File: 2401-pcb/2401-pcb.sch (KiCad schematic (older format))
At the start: 100 parts, among them J1 Load Cell, J2 Conn_ARM_JTAG_SWD_10, J3 Conn_01x04_Male, Q1 SFH3710, Q2 SFH3710, SW1 SW_SPDT, U1 LIS3DH, U10 MCP6001U, U11 MCP6001U, U2 VL6180X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

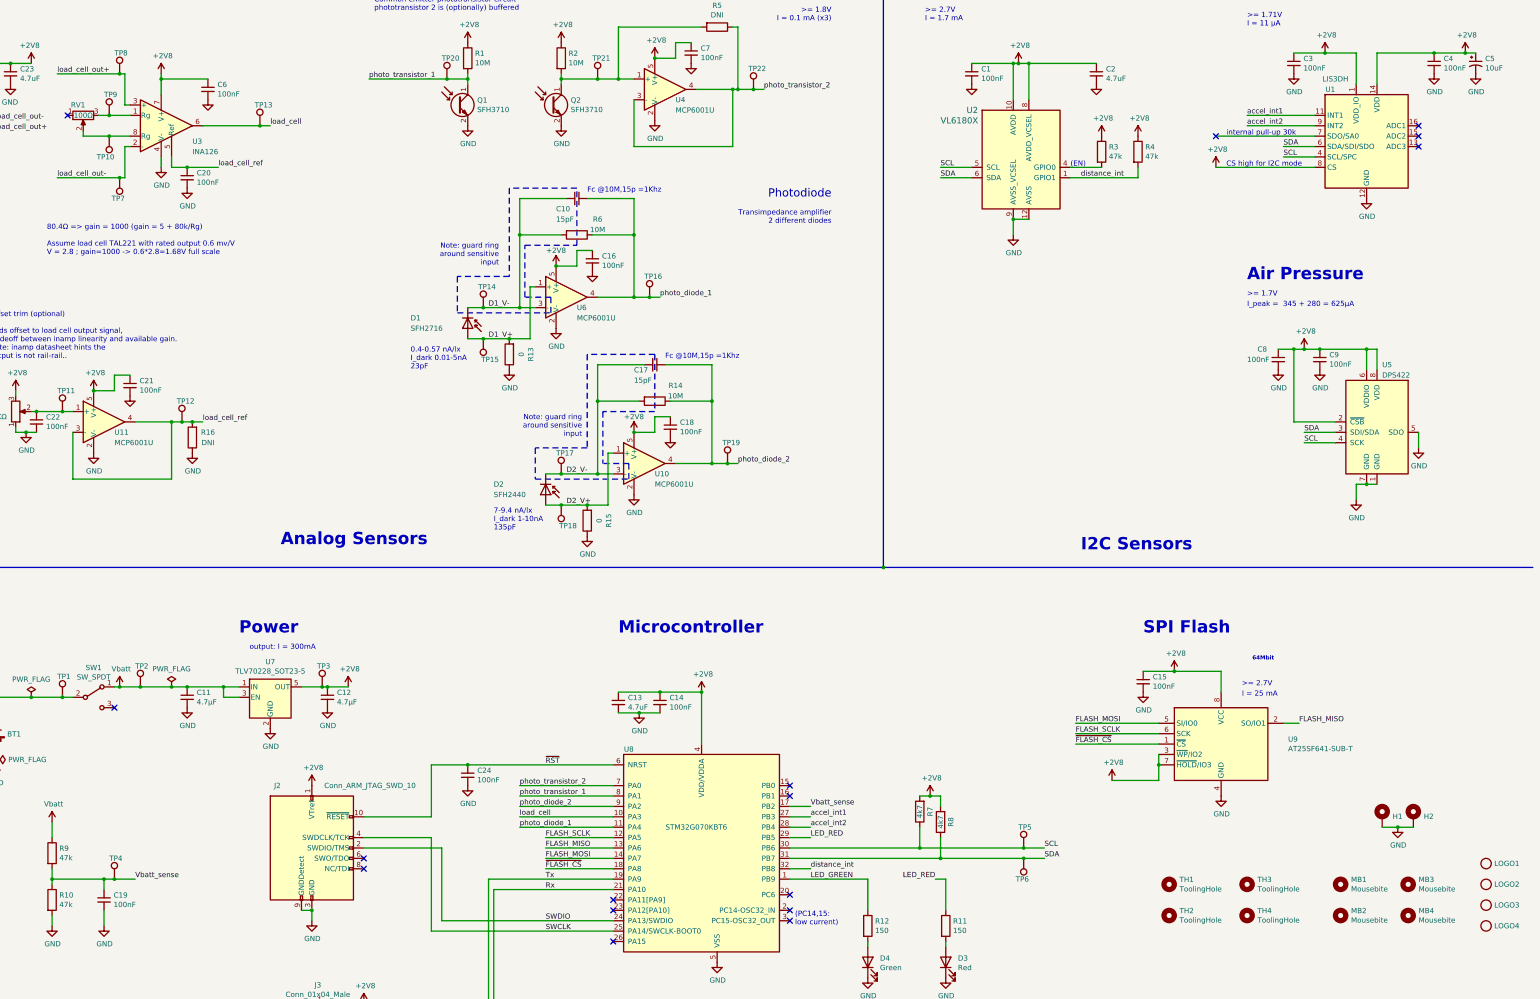
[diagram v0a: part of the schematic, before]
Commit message: PCB: add Final production BOM
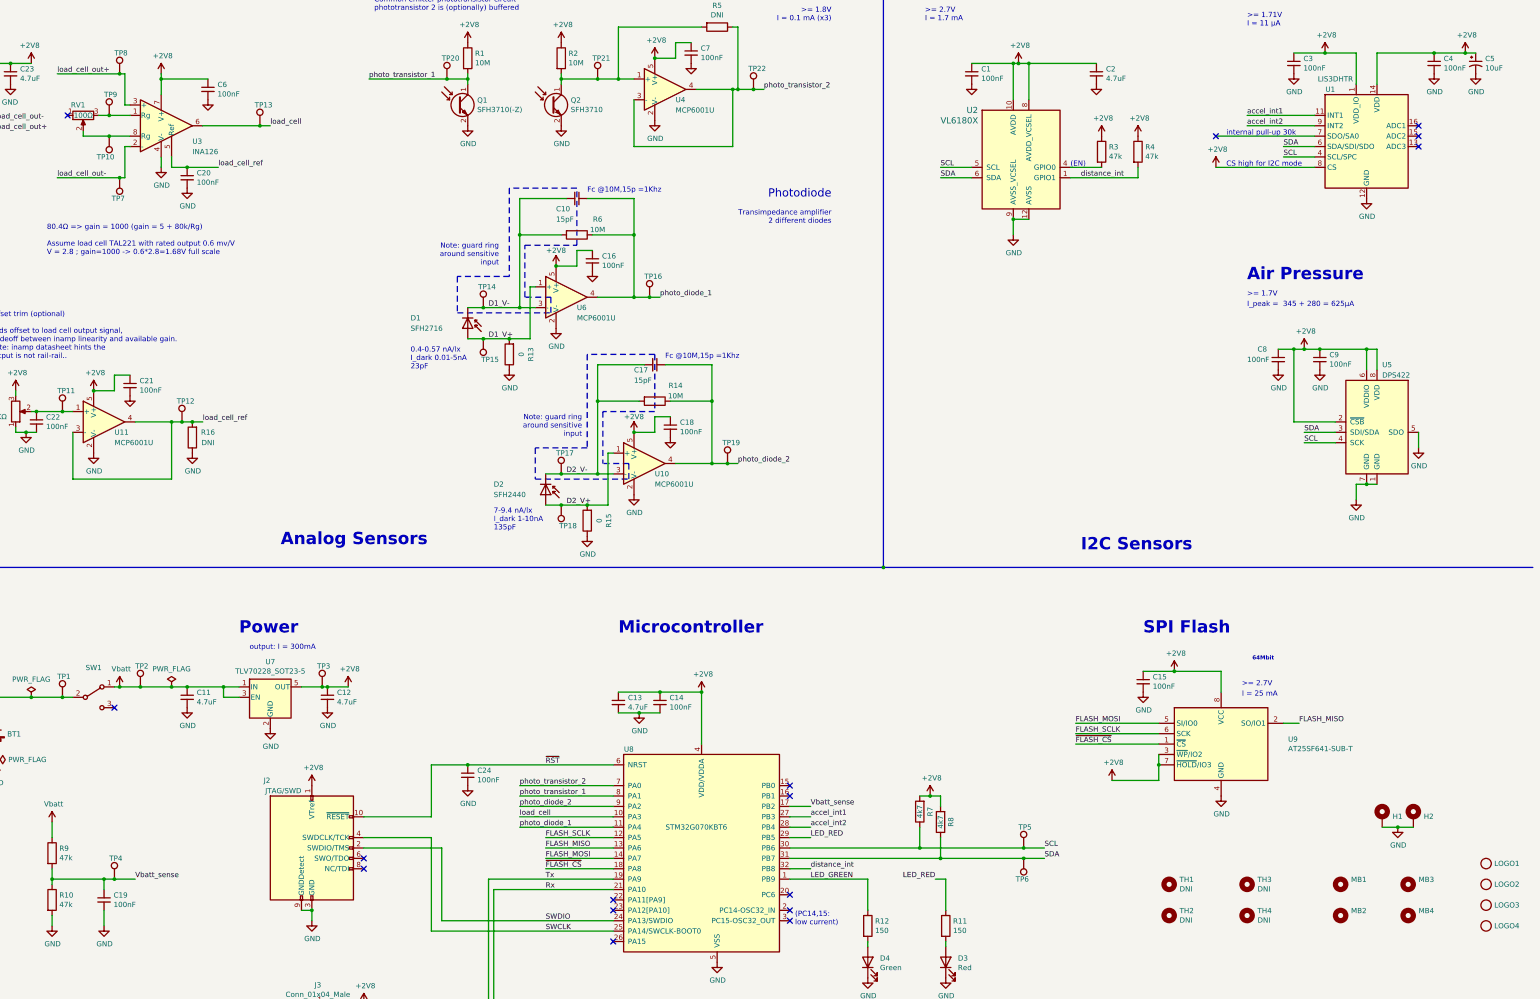
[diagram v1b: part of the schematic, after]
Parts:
- C11, C12: value 4.7µF -> 4.7uF
- D1: Farnell (none) -> 2981722; MPN (none) -> SFH 2716
- D2: Farnell (none) -> 2981709; MPN (none) -> SFH 2440
- H1, H2: value MountingHole_Pad -> DNI
- J1: Farnell (none) -> 9492631; MPN (none) -> S4B-PH-SM4-TB(LF)(SN)
- J2: value Conn_ARM_JTAG_SWD_10 -> JTAG/SWD; MPN (none) -> 20021521-00010T1LF; Note (none) -> Jitter has large amount in stock..
- LOGO1, LOGO2, LOGO3, LOGO4: value LOGO -> DNI
- MB1, MB2, MB3, MB4: value Mousebite -> DNI
- Q1: value SFH3710 -> SFH3710(-Z); Alternative (none) -> SFH3710; Farnell (none) -> 2981749; MPN (none) -> SFH3710-Z
- Q2: Farnell (none) -> 1573490; MPN (none) -> SFH3710
- SW1: Farnell (none) -> 1608080; MPN (none) -> 09.03201.02
- TH1, TH2, TH3, TH4: value ToolingHole -> DNI
- U1: value LIS3DH -> LIS3DHTR; Farnell (none) -> 2253507; MPN (none) -> LIS3DHTR; Mouser (none) -> 511-LIS3DHTR; NOTE (none) -> NOT the same as LIS3DHH !!
- U2: Farnell (none) -> 2462820; MPN (none) -> VL6180XV0NR/1
- U3: MPN (none) -> INA126E
- U5: Farnell (none) -> 2986299; MPN (none) -> DPS422XTSA1
- U7: Farnell (none) -> 2492371; MPN (none) -> TLV70228DBVT
- U8: Farnell (none) -> 3365394; MPN (none) -> STM32G070KBT6; Mouser (none) -> 511-STM32G070KBT6
- U9: Farnell (none) -> 2988514; MPN (none) -> AT25SF641-SUB-T
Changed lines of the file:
@@
 F 2 "Package_SO:SOIC-8_3.9x4.9mm_P1.27mm" H 13050 7450 50  0001 C CNN
 F 3 "http://www.farnell.com/datasheets/2720345.pdf" H 13050 8050 50  0001 C CNN
+F 4 "AT25SF641-SUB-T" H 13050 8050 50  0001 C CNN "MPN"
+F 5 "2988514" H 13050 8050 50  0001 C CNN "Farnell"
 	1    13050 8050
 	1    0    0    -1
@@
 P 4450 7600
 F 0 "C12" H 4542 7646 50  0000 L CNN
-F 1 "4.7µF" H 4542 7555 50  0000 L CNN
+F 1 "4.7uF" H 4542 7555 50  0000 L CNN
 F 2 "Capacitor_SMD:C_0805_2012Metric" H 4450 7600 50  0001 C CNN
 F 3 "~" H 4450 7600 50  0001 C CNN
@@
 P 3100 7600
 F 0 "C11" H 3192 7646 50  0000 L CNN
-F 1 "4.7µF" H 3192 7555 50  0000 L CNN
+F 1 "4.7uF" H 3192 7555 50  0000 L CNN
 F 2 "Capacitor_SMD:C_0805_2012Metric" H 3100 7600 50  0001 C CNN
 F 3 "~" H 3100 7600 50  0001 C CNN
@@
 F 2 "Package_TO_SOT_SMD:SOT-23-5" H 3900 7925 50  0001 C CIN
 F 3 "http://www.ti.com/lit/ds/symlink/tlv702.pdf" H 3900 7650 50  0001 C CNN
+F 4 "TLV70228DBVT" H 3900 7600 50  0001 C CNN "MPN"
+F 5 "2492371" H 3900 7600 50  0001 C CNN "Farnell"
 	1    3900 7600
 	1    0    0    -1
@@
 P 2200 7600
 F 0 "SW1" H 2200 7885 50  0000 C CNN
-F 1 "SW_SPDT" H 2200 7794 50  0000 C CNN
+F 1 "SW_SPDT" H 2200 7794 50  0001 C CNN
 F 2 "Jitter_Footprints:slide_switch_09.03201.02" H 2200 7600 50  0001 C CNN
 F 3 "~" H 2200 7600 50  0001 C CNN
+F 4 "09.03201.02" H 2200 7600 50  0001 C CNN "MPN"
+F 5 "1608080" H 2200 7600 50  0001 C CNN "Farnell"
 	1    2200 7600
 	1    0    0    -1
@@
 U 1 1 5E58D766
 P 4300 9050
-F 0 "J2" H 4000 9650 50  0000 R CNN
-F 1 "Conn_ARM_JTAG_SWD_10" H 5300 9650 50  0000 R CNN
+F 0 "J2" H 3900 9700 50  0000 R CNN
+F 1 "JTAG/SWD" H 4200 9600 50  0000 R CNN
 F 2 "Jitter_Footprints:connector_jtag_10pin_shrouded" H 4300 9050 50  0001 C CNN
 F 3 "http://infocenter.arm.com/help/topic/com.arm.doc.ddi0314h/DDI0314H_coresight_components_trm.pdf" V 3950 7800 50  0001 C CNN
+F 4 "20021521-00010T1LF" H 4300 9050 50  0001 C CNN "MPN"
+F 5 "Jitter has large amount in stock.." H 4300 9050 50  0001 C CNN "Note"
 	1    4300 9050
 	1    0    0    -1
@@
 P 14600 8750
 F 0 "H1" H 14700 8753 50  0000 L CNN
-F 1 "MountingHole_Pad" H 14700 8708 50  0001 L CNN
+F 1 "DNI" H 14700 8708 50  0001 L CNN
 F 2 "MountingHole:MountingHole_4.5mm_Pad_Via" H 14600 8750 50  0001 C CNN
 F 3 "~" H 14600 8750 50  0001 C CNN
@@
 P 14900 8750
 F 0 "H2" H 15000 8753 50  0000 L CNN
-F 1 "MountingHole_Pad" H 15000 8708 50  0001 L CNN
+F 1 "DNI" H 15000 8708 50  0001 L CNN
 F 2 "MountingHole:MountingHole_4.5mm_Pad_Via" H 14900 8750 50  0001 C CNN
 F 3 "~" H 14900 8750 50  0001 C CNN
@@
 F 3 "https://www.st.com/resource/en/datasheet/stm32g070kb.pdf" H 8200 8850 50  0001 C CNN
 F 4 "https://www.st.com/content/ccc/resource/technical/document/reference_manual/group0/fd/a3/20/58/ac/b0/48/23/DM00463896/files/DM00463896.pdf/jcr:content/translations/en.DM00463896.pdf" H 7900 8850 50  0001 C CNN "Manual"
+F 5 "STM32G070KBT6" H 8050 8850 50  0001 C CNN "MPN"
+F 6 "511-STM32G070KBT6" H 8050 8850 50  0001 C CNN "Mouser"
+F 7 "3365394" H 8050 8850 50  0001 C CNN "Farnell"
 	1    8050 8850
 	1    0    0    -1
@@
 P 15600 9200
 F 0 "LOGO1" H 15678 9200 50  0000 L CNN
-F 1 "LOGO" H 15678 9155 50  0001 L CNN
+F 1 "DNI" H 15678 9155 50  0001 L CNN
 F 2 "Jitter_Logos:Jitter" H 15600 9200 50  0001 C CNN
 F 3 "" H 15600 9200 50  0001 C CNN
@@
 P 15600 9400
 F 0 "LOGO2" H 15678 9400 50  0000 L CNN
-F 1 "LOGO" H 15678 9355 50  0001 L CNN
+F 1 "DNI" H 15678 9355 50  0001 L CNN
 F 2 "Jitter_Logos:Symbol_Jitter-Icon_CopperAndSilkScreenTop" H 15600 9400 50  0001 C CNN
 F 3 "" H 15600 9400 50  0001 C CNN
@@
 P 14200 9400
 F 0 "MB1" H 14300 9446 50  0000 L CNN
-F 1 "Mousebite" H 14300 9355 50  0000 L CNN
+F 1 "DNI" H 14300 9355 50  0001 L CNN
 F 2 "Jitter_Footprints:MouseBite_3.5mmx2.2mm_breakaway" H 14200 9400 50  0001 C CNN
 F 3 "~" H 14200 9400 50  0001 C CNN
@@
 P 14200 9700
 F 0 "MB2" H 14300 9746 50  0000 L CNN
-F 1 "Mousebite" H 14300 9655 50  0000 L CNN
+F 1 "DNI" H 14300 9655 50  0001 L CNN
 F 2 "Jitter_Footprints:MouseBite_3.5mmx2.2mm_breakaway" H 14200 9700 50  0001 C CNN
 F 3 "~" H 14200 9700 50  0001 C CNN
@@
 P 14850 9400
 F 0 "MB3" H 14950 9446 50  0000 L CNN
-F 1 "Mousebite" H 14950 9355 50  0000 L CNN
+F 1 "DNI" H 14950 9355 50  0001 L CNN
 F 2 "Jitter_Footprints:MouseBite_3.5mmx2.2mm_breakaway" H 14850 9400 50  0001 C CNN
 F 3 "~" H 14850 9400 50  0001 C CNN
@@
 P 14850 9700
 F 0 "MB4" H 14950 9746 50  0000 L CNN
-F 1 "Mousebite" H 14950 9655 50  0000 L CNN
+F 1 "DNI" H 14950 9655 50  0001 L CNN
 F 2 "Jitter_Footprints:MouseBite_3.5mmx2.2mm_breakaway" H 14850 9700 50  0001 C CNN
 F 3 "~" H 14850 9700 50  0001 C CNN
@@
 P 12550 9400
 F 0 "TH1" H 12650 9446 50  0000 L CNN
-F 1 "ToolingHole" H 12650 9355 50  0000 L CNN
+F 1 "DNI" H 12650 9355 50  0000 L CNN
 F 2 "Jitter_Footprints:Tooling_hole_4mm_4.04mm_paste" H 12550 9400 50  0001 C CNN
 F 3 "~" H 12550 9400 50  0001 C CNN
@@
 P 12550 9700
 F 0 "TH2" H 12650 9746 50  0000 L CNN
-F 1 "ToolingHole" H 12650 9655 50  0000 L CNN
+F 1 "DNI" H 12650 9655 50  0000 L CNN
 F 2 "Jitter_Footprints:Tooling_hole_4mm_4.04mm_paste" H 12550 9700 50  0001 C CNN
 F 3 "~" H 12550 9700 50  0001 C CNN
@@
 P 13300 9700
 F 0 "TH4" H 13400 9746 50  0000 L CNN
-F 1 "ToolingHole" H 13400 9655 50  0000 L CNN
+F 1 "DNI" H 13400 9655 50  0000 L CNN
 F 2 "Jitter_Footprints:Tooling_hole_4mm_4.04mm_paste" H 13300 9700 50  0001 C CNN
 F 3 "~" H 13300 9700 50  0001 C CNN
@@
 P 13300 9400
 F 0 "TH3" H 13400 9446 50  0000 L CNN
-F 1 "ToolingHole" H 13400 9355 50  0000 L CNN
+F 1 "DNI" H 13400 9355 50  0000 L CNN
 F 2 "Jitter_Footprints:Tooling_hole_4mm_4.04mm_paste" H 13300 9400 50  0001 C CNN
 F 3 "~" H 13300 9400 50  0001 C CNN
@@
 P 15600 9600
 F 0 "LOGO3" H 15678 9600 50  0000 L CNN
-F 1 "LOGO" H 15678 9555 50  0001 L CNN
+F 1 "DNI" H 15678 9555 50  0001 L CNN
 F 2 "Jitter_Logos:Jitter" H 15600 9600 50  0001 C CNN
 F 3 "" H 15600 9600 50  0001 C CNN
@@
 P 15600 9800
 F 0 "LOGO4" H 15678 9800 50  0000 L CNN
-F 1 "LOGO" H 15678 9755 50  0001 L CNN
+F 1 "DNI" H 15678 9755 50  0001 L CNN
 F 2 "Jitter_Logos:Symbol_Jitter-Icon_CopperAndSilkScreenTop" H 15600 9800 50  0001 C CNN
 F 3 "" H 15600 9800 50  0001 C CNN
@@
 F 2 "Jitter_Footprints:VL6180X" H 11100 3100 118 0001 C CNN
 F 3 "http://www.farnell.com/datasheets/2308888.pdf" H 11100 3100 118 0001 C CNN
+F 4 "VL6180XV0NR/1" H 11100 2400 50  0001 C CNN "MPN"
+F 5 "2462820" H 11100 2400 50  0001 C CNN "Farnell"
 	1    11100 2400
 	1    0    0    -1
@@
 F 2 "Jitter_Footprints:JST_PH_S4B-PH-SM4-TB_1x04-1MP_P2.00mm_Horizontal" H 900 2050 50  0001 C CNN
 F 3 "~" H 900 2050 50  0001 C CNN
+F 4 "S4B-PH-SM4-TB(LF)(SN)" H 900 2050 50  0001 C CNN "MPN"
+F 5 "9492631" H 900 2050 50  0001 C CNN "Farnell"
 	1    900  2050
 	-1   0    0    -1
@@
 F 3 "http://www.ti.com/lit/ds/symlink/ina126.pdf" H 2950 2100 50  0001 C CNN
 F 4 "3004490" H 2850 2100 50  0001 C CNN "Farnell"
+F 5 "INA126E" H 2850 2100 50  0001 C CNN "MPN"
 	1    2850 2100
 	1    0    0    -1
@@
 F 2 "OptoDevice:Osram_SMD-DIL2_4.5x4.0mm" H 6550 5825 50  0001 C CNN
 F 3 "http://www.osram-os.com/Graphics/XPic2/00231367_0.pdf/SFH%202440.pdf" H 6500 5650 50  0001 C CNN
+F 4 "SFH 2440" V 6550 5650 50  0001 C CNN "MPN"
+F 5 "2981709" V 6550 5650 50  0001 C CNN "Farnell"
 	1    6550 5650
 	0    1    1    0
@@
 F 2 "Diode_SMD:D_0805_2012Metric_Pad1.15x1.40mm_HandSolder" H 6800 2000 50  0001 C CNN
 F 3 "http://www.farnell.com/datasheets/43564.pdf" H 6600 1900 50  0001 C CNN
+F 4 "SFH3710" H 6600 1900 50  0001 C CNN "MPN"
+F 5 "1573490" H 6600 1900 50  0001 C CNN "Farnell"
 	1    6600 1900
 	1    0    0    -1
@@
 P 5700 1900
 F 0 "Q1" H 5891 1946 50  0000 L CNN
-F 1 "SFH3710" H 5891 1855 50  0000 L CNN
+F 1 "SFH3710(-Z)" H 5891 1855 50  0000 L CNN
 F 2 "Diode_SMD:D_0805_2012Metric_Pad1.15x1.40mm_HandSolder" H 5900 2000 50  0001 C CNN
 F 3 "http://www.farnell.com/datasheets/43564.pdf" H 5700 1900 50  0001 C CNN
+F 4 "SFH3710-Z" H 5700 1900 50  0001 C CNN "MPN"
+F 5 "2981749" H 5700 1900 50  0001 C CNN "Farnell"
+F 6 "SFH3710" H 5700 1900 50  0001 C CNN "Alternative"
 	1    5700 1900
 	1    0    0    -1
@@
 F 2 "Diode_SMD:D_0805_2012Metric" H 5750 4050 50  0001 C CNN
 F 3 "http://www.farnell.com/datasheets/2711855.pdf" H 5750 4050 50  0001 C CNN
+F 4 "SFH 2716" V 5800 4050 50  0001 C CNN "MPN"
+F 5 "2981722" V 5800 4050 50  0001 C CNN "Farnell"
 	1    5800 4050
 	0    1    1    0
@@
 P 14450 2200
 F 0 "U1" H 14100 2650 50  0000 C CNN
-F 1 "LIS3DH" H 14150 2750 50  0000 C CNN
+F 1 "LIS3DHTR" H 14150 2750 50  0000 C CNN
 F 2 "Package_LGA:LGA-16_3x3mm_P0.5mm_LayoutBorder3x5y" H 14550 1150 50  0001 C CNN
 F 3 "https://www.st.com/resource/en/datasheet/cd00274221.pdf" H 14250 2100 50  0001 C CNN
+F 4 "LIS3DHTR" H 14450 2200 50  0001 C CNN "MPN"
+F 5 "511-LIS3DHTR" H 14450 2200 50  0001 C CNN "Mouser"
+F 6 "2253507" H 14450 2200 50  0001 C CNN "Farnell"
+F 7 "NOT the same as LIS3DHH !!" H 14450 2200 50  0001 C CNN "NOTE"
 	1    14450 2200
 	1    0    0    -1
@@
 F 2 "Package_LGA:Bosch_LGA-8_2x2.5mm_P0.65mm_ClockwisePinNumbering" H 14550 5900 118 0001 C CNN
 F 3 "https://www.infineon.com/dgdl/Infineon-DPS422-DS-v01_03-EN.pdf?fileId=5546d46264fee02f01650249502c1ddf" H 14550 5900 118 0001 C CNN
+F 4 "DPS422XTSA1" H 14550 5050 50  0001 C CNN "MPN"
+F 5 "2986299" H 14550 5050 50  0001 C CNN "Farnell"
 	1    14550 5050
 	1    0    0    -1

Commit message: Changes for production at aisler
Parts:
- TH1, TH2, TH3, TH4: footprint Jitter_Footprints:Tooling_hole_4mm_4.04mm_paste -> Jitter_Footprints:Tooling_hole_4.1mm_aisler
- U9: footprint Package_SO:SOIC-8_3.9x4.9mm_P1.27mm -> Package_SO:SOIC-8_5.275x5.275mm_P1.27mm
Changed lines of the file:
@@
 F 0 "U9" H 13694 8096 50  0000 L CNN
 F 1 "AT25SF641-SUB-T" H 13694 8005 50  0000 L CNN
-F 2 "Package_SO:SOIC-8_3.9x4.9mm_P1.27mm" H 13050 7450 50  0001 C CNN
+F 2 "Package_SO:SOIC-8_5.275x5.275mm_P1.27mm" H 13050 7450 50  0001 C CNN
 F 3 "http://www.farnell.com/datasheets/2720345.pdf" H 13050 8050 50  0001 C CNN
 F 4 "AT25SF641-SUB-T" H 13050 8050 50  0001 C CNN "MPN"
@@
 F 0 "TH1" H 12650 9446 50  0000 L CNN
 F 1 "DNI" H 12650 9355 50  0000 L CNN
-F 2 "Jitter_Footprints:Tooling_hole_4mm_4.04mm_paste" H 12550 9400 50  0001 C CNN
+F 2 "Jitter_Footprints:Tooling_hole_4.1mm_aisler" H 12550 9400 50  0001 C CNN
 F 3 "~" H 12550 9400 50  0001 C CNN
 	1    12550 9400
@@
 F 0 "TH2" H 12650 9746 50  0000 L CNN
 F 1 "DNI" H 12650 9655 50  0000 L CNN
-F 2 "Jitter_Footprints:Tooling_hole_4mm_4.04mm_paste" H 12550 9700 50  0001 C CNN
+F 2 "Jitter_Footprints:Tooling_hole_4.1mm_aisler" H 12550 9700 50  0001 C CNN
 F 3 "~" H 12550 9700 50  0001 C CNN
 	1    12550 9700
@@
 F 0 "TH4" H 13400 9746 50  0000 L CNN
 F 1 "DNI" H 13400 9655 50  0000 L CNN
-F 2 "Jitter_Footprints:Tooling_hole_4mm_4.04mm_paste" H 13300 9700 50  0001 C CNN
+F 2 "Jitter_Footprints:Tooling_hole_4.1mm_aisler" H 13300 9700 50  0001 C CNN
 F 3 "~" H 13300 9700 50  0001 C CNN
 	1    13300 9700
@@
 F 0 "TH3" H 13400 9446 50  0000 L CNN
 F 1 "DNI" H 13400 9355 50  0000 L CNN
-F 2 "Jitter_Footprints:Tooling_hole_4mm_4.04mm_paste" H 13300 9400 50  0001 C CNN
+F 2 "Jitter_Footprints:Tooling_hole_4.1mm_aisler" H 13300 9400 50  0001 C CNN
 F 3 "~" H 13300 9400 50  0001 C CNN
 	1    13300 9400

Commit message: PCb changes
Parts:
- R1: value 10M -> 1M
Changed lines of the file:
@@
 P 5800 1450
 F 0 "R1" H 5870 1496 50  0000 L CNN
-F 1 "10M" H 5870 1405 50  0000 L CNN
+F 1 "1M" H 5870 1405 50  0000 L CNN
 F 2 "Resistor_SMD:R_0805_2012Metric_Pad1.15x1.40mm_HandSolder" V 5730 1450 50  0001 C CNN
 F 3 "~" H 5800 1450 50  0001 C CNN
